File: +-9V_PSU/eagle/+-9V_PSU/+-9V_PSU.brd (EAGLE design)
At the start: 93.7 x 71.1 mm, 24 parts, among them IC1 7809TV, IC2 7909TV

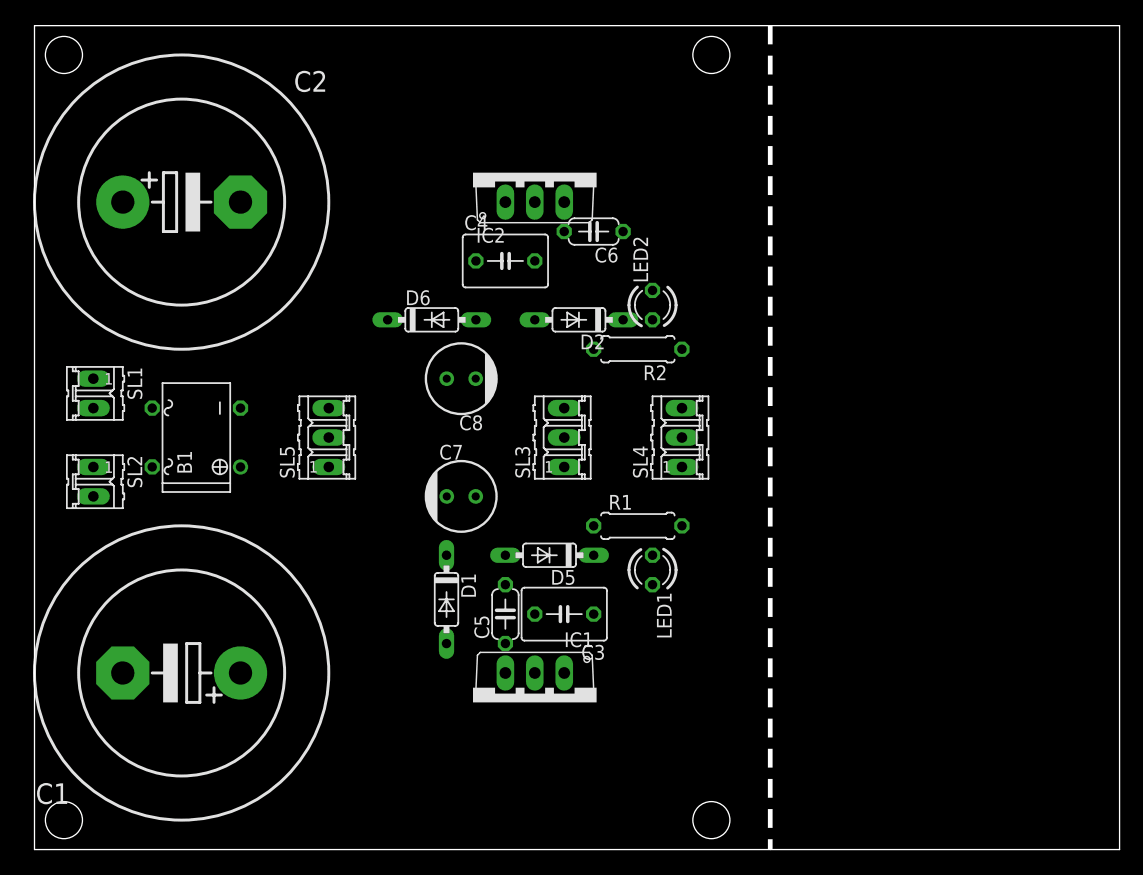
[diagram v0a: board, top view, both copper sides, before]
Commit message: +-9V PSU Board design
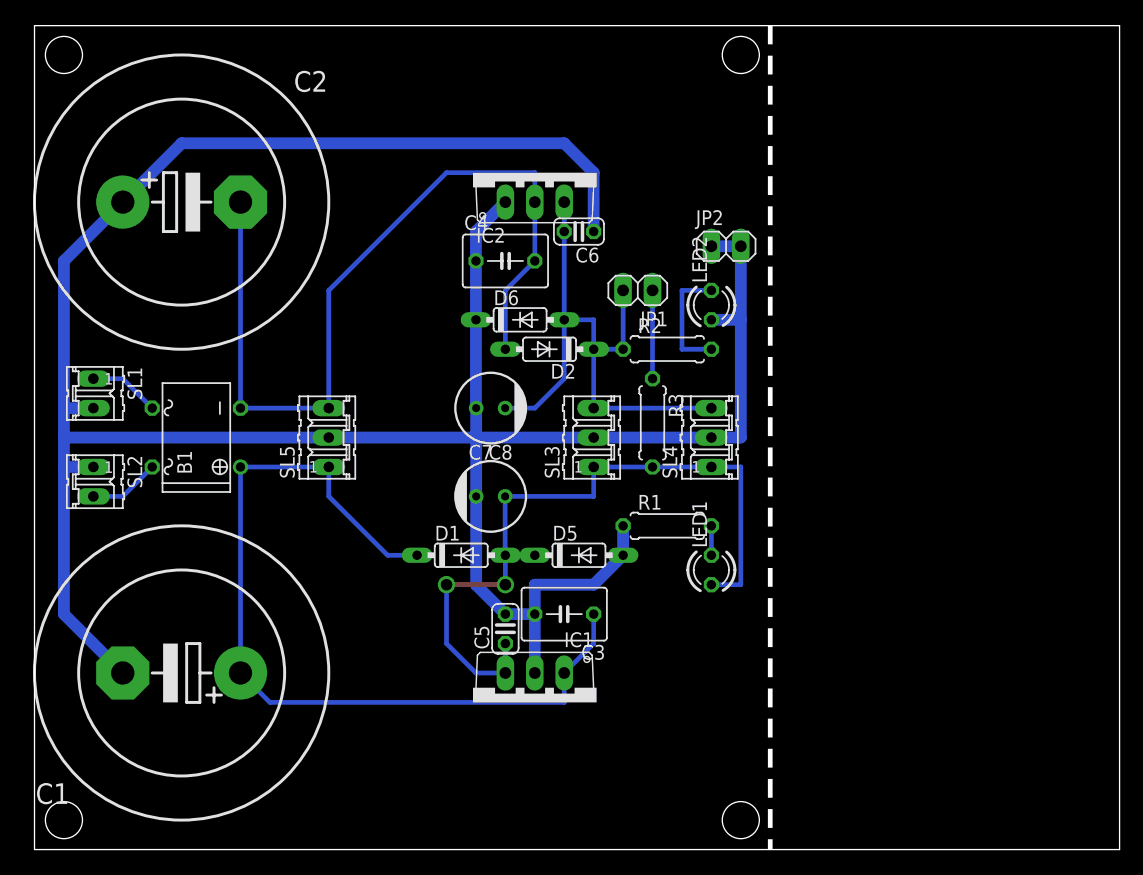
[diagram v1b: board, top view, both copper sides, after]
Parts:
- added JP1: LED, pinhead:1X02
- added JP2: TP_GND, pinhead:1X02
- added R3: 10k, rcl:0207/7
- C5, C6: device rcl:C050-024X044 -> rcl:C025-024X044
- SL1: value (none) -> ACIN1
- SL2: value (none) -> ACIN2
- SL3, SL4: value (none) -> DC9V
- SL5: value (none) -> DC12V
- moved D6 7.62 mm to (41.9, 45.7)
- moved LED1 5.08 mm to (58.4, 24.1), turned to 90 degrees
- moved LED2 5.08 mm to (58.4, 47.0)
- moved D1 4.02 mm to (36.8, 25.4), turned to 0 degrees
- moved C8 3.59 mm to (39.4, 38.1)
- moved D2 3.59 mm to (44.5, 43.2)
- moved C7 2.54 mm to (39.4, 30.5)
- moved D5 2.54 mm to (47.0, 25.4), turned to 0 degrees
- moved R1 2.54 mm to (54.6, 27.9)
- moved R2 2.54 mm to (54.6, 43.2), turned to 0 degrees
- moved SL3 2.54 mm to (48.3, 35.6)
- moved SL4 2.54 mm to (58.4, 35.6)
- moved C5 1.27 mm to (40.6, 19.1)
- moved C6 1.27 mm to (47.0, 53.3)
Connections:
- new net N$2: JP1.1, R3.1
- net +9V: now also R3.2
- net -9V: now also JP1.2, R2.1; no longer LED2.K
- net GND: now also JP2.1, JP2.2, LED2.A; no longer R2.2
- net N$1: now also LED2.K, R2.2; no longer LED2.A, R2.1
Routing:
- net GND: track 0.00 -> 237.9 mm
- net +12V: track 0.00 -> 75.3 mm
- net -12V: track 0.00 -> 73.8 mm
- net +9V: track 0.00 -> 64.6 mm, vias 0 -> 2
- net -9V: track 0.00 -> 49.3 mm
- net N$1: track 0.00 -> 10.2 mm
- net N$2: track 0.00 -> 7.62 mm
- net N$6: track 0.00 -> 6.13 mm
- net N$4: track 0.00 -> 6.13 mm
- net N$3: track 0.00 -> 2.54 mm

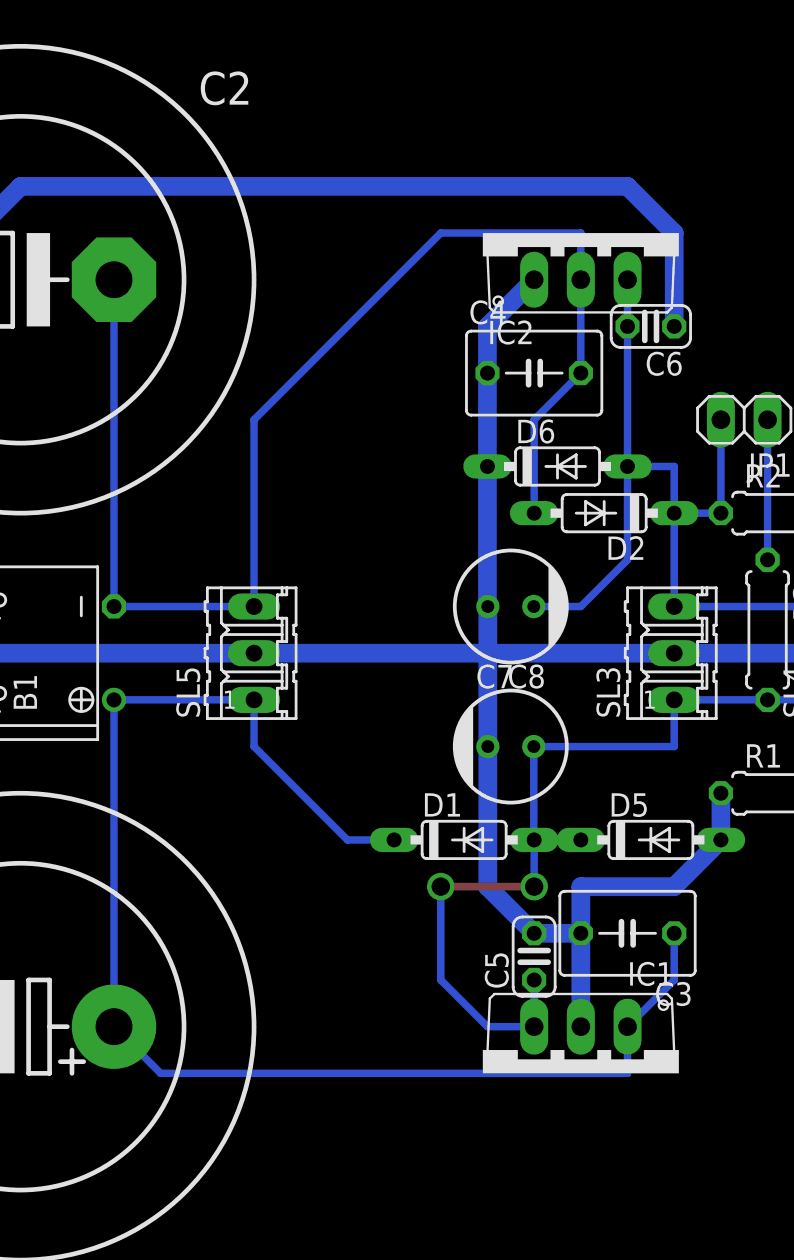
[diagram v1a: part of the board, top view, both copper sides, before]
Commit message: +-9V_PSU Update
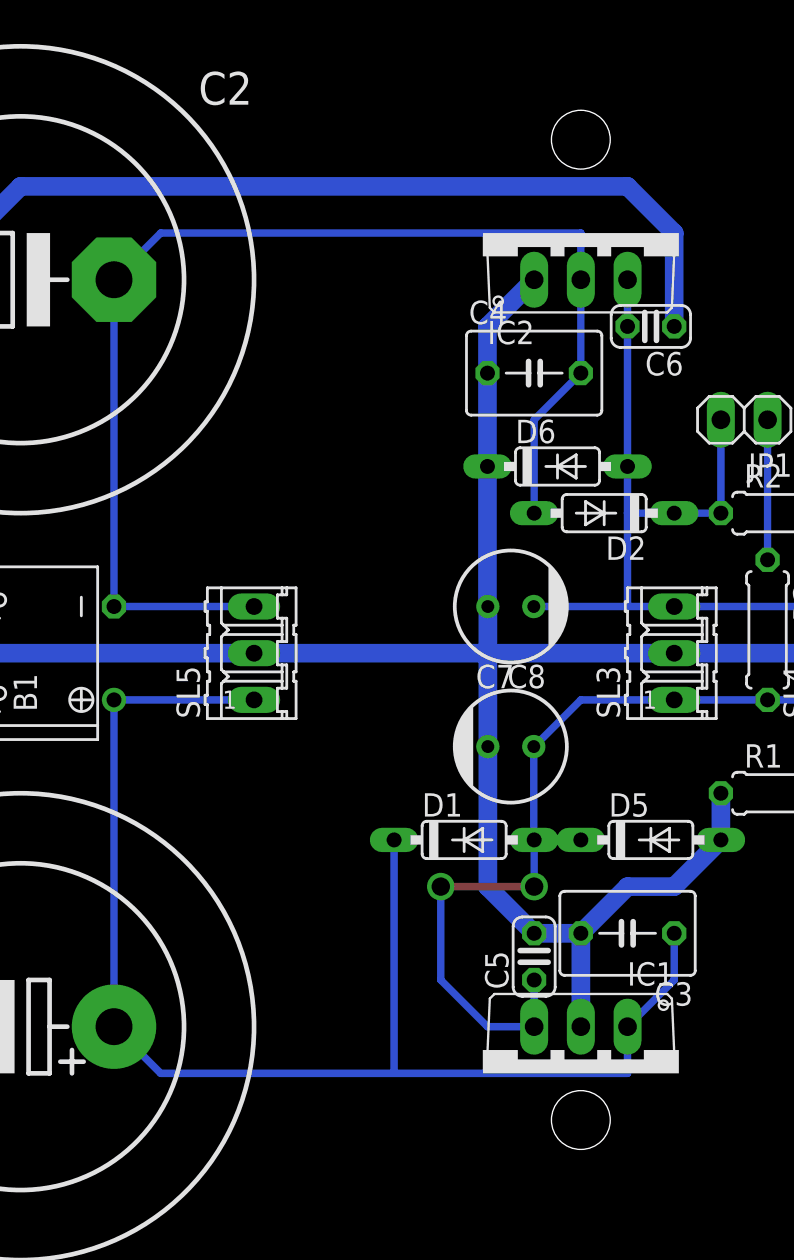
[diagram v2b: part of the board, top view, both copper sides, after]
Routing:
- net -12V: track 73.8 -> 68.1 mm
- net -9V: track 49.3 -> 45.7 mm
- net GND: track 237.9 -> 236.4 mm
- net +9V: track 64.6 -> 63.1 mm
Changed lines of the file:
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@@
 <layer number="98" name="Guide" color="6" fill="1" visible="no" active="no"/>
 <layer number="99" name="SpiceOrder" color="5" fill="1" visible="no" active="no"/>
-<layer number="100" name="Grid" color="11" fill="1" visible="yes" active="yes"/>
+<layer number="100" name="Grid" color="11" fill="1" visible="no" active="yes"/>
 <layer number="200" name="200bmp" color="1" fill="10" visible="no" active="no"/>
 <layer number="201" name="tNamesOnPCB" color="5" fill="1" visible="yes" active="yes"/>
@@
 <hole x="60.96" y="2.54" drill="3.2"/>
 <dimension x1="0" y1="0" x2="63.5" y2="0" x3="31.75" y3="-5.08" textsize="1.778" layer="20"/>
+<hole x="43.18" y="10.16" drill="3.2"/>
+<hole x="43.18" y="63.5" drill="3.2"/>
 </plain>
 <attributes>
@@
 <wire x1="45.72" y1="60.96" x2="12.7" y2="60.96" width="1.016" layer="16"/>
 <wire x1="12.7" y1="60.96" x2="7.62" y2="55.88" width="1.016" layer="16"/>
-<wire x1="43.18" y1="20.32" x2="43.18" y2="22.86" width="1.016" layer="16"/>
-<wire x1="43.18" y1="22.86" x2="48.26" y2="22.86" width="1.016" layer="16"/>
 <wire x1="48.26" y1="22.86" x2="50.8" y2="25.4" width="1.016" layer="16"/>
 <contactref element="LED2" pad="A"/>
@@
 <wire x1="58.42" y1="52.07" x2="60.96" y2="52.07" width="1.016" layer="16"/>
 <wire x1="60.96" y1="52.07" x2="60.96" y2="45.72" width="1.016" layer="16"/>
+<wire x1="43.18" y1="20.32" x2="45.72" y2="22.86" width="1.016" layer="16"/>
+<wire x1="45.72" y1="22.86" x2="48.26" y2="22.86" width="1.016" layer="16"/>
 </signal>
 <signal name="-9V">
@@
 <wire x1="45.72" y1="55.88" x2="45.72" y2="53.34" width="0.4064" layer="16"/>
 <wire x1="45.72" y1="45.72" x2="45.72" y2="53.34" width="0.4064" layer="16"/>
-<wire x1="40.62" y1="38.1" x2="43.18" y2="38.1" width="0.4064" layer="16"/>
-<wire x1="43.18" y1="38.1" x2="45.72" y2="40.64" width="0.4064" layer="16"/>
-<wire x1="45.72" y1="40.64" x2="45.72" y2="45.72" width="0.4064" layer="16"/>
+<wire x1="45.72" y1="43.18" x2="45.72" y2="45.72" width="0.4064" layer="16"/>
 <wire x1="48.26" y1="38.1" x2="58.42" y2="38.1" width="0.4064" layer="16"/>
 <contactref element="R2" pad="1"/>
-<wire x1="45.72" y1="45.72" x2="48.26" y2="45.72" width="0.4064" layer="16"/>
-<wire x1="48.26" y1="45.72" x2="48.26" y2="43.18" width="0.4064" layer="16"/>
-<wire x1="48.26" y1="43.18" x2="48.26" y2="38.1" width="0.4064" layer="16"/>
 <contactref element="JP1" pad="2"/>
 <wire x1="50.8" y1="43.18" x2="50.8" y2="48.26" width="0.4064" layer="16"/>
 <wire x1="50.8" y1="43.18" x2="48.26" y2="43.18" width="0.4064" layer="16"/>
+<wire x1="48.26" y1="43.18" x2="45.72" y2="43.18" width="0.4064" layer="16"/>
+<wire x1="48.26" y1="38.1" x2="45.72" y2="38.1" width="0.4064" layer="16"/>
+<wire x1="45.72" y1="38.1" x2="40.62" y2="38.1" width="0.4064" layer="16"/>
+<wire x1="45.72" y1="43.18" x2="45.72" y2="38.1" width="0.4064" layer="16"/>
 </signal>
 <signal name="+9V">
@@
 <wire x1="40.62" y1="30.48" x2="40.62" y2="25.42" width="0.4064" layer="16"/>
 <wire x1="40.62" y1="25.42" x2="40.64" y2="25.4" width="0.4064" layer="16"/>
-<wire x1="40.62" y1="30.48" x2="48.26" y2="30.48" width="0.4064" layer="16"/>
-<wire x1="48.26" y1="30.48" x2="48.26" y2="33.02" width="0.4064" layer="16"/>
 <wire x1="43.18" y1="25.4" x2="40.64" y2="25.4" width="0.4064" layer="16"/>
 <contactref element="R3" pad="2"/>
@@
 <via x="40.64" y="22.86" extent="1-16" drill="1" shape="square"/>
 <via x="35.56" y="22.86" extent="1-16" drill="1" shape="square"/>
+<wire x1="40.62" y1="30.48" x2="40.64" y2="30.48" width="0.4064" layer="16"/>
+<wire x1="40.64" y1="30.48" x2="43.18" y2="33.02" width="0.4064" layer="16"/>
+<wire x1="43.18" y1="33.02" x2="48.26" y2="33.02" width="0.4064" layer="16"/>
 </signal>
 <signal name="N$3">
@@
 <wire x1="17.78" y1="33.02" x2="25.4" y2="33.02" width="0.4064" layer="16"/>
 <wire x1="17.78" y1="15.24" x2="20.32" y2="12.7" width="0.4064" layer="16"/>
-<wire x1="20.32" y1="12.7" x2="45.72" y2="12.7" width="0.4064" layer="16"/>
+<wire x1="20.32" y1="12.7" x2="33.02" y2="12.7" width="0.4064" layer="16"/>
+<wire x1="33.02" y1="12.7" x2="45.72" y2="12.7" width="0.4064" layer="16"/>
 <wire x1="45.72" y1="12.7" x2="45.72" y2="15.24" width="0.4064" layer="16"/>
 <wire x1="17.78" y1="15.24" x2="17.78" y2="33.02" width="0.4064" layer="16"/>
-<wire x1="25.4" y1="33.02" x2="25.4" y2="30.48" width="0.4064" layer="16"/>
-<wire x1="25.4" y1="30.48" x2="30.48" y2="25.4" width="0.4064" layer="16"/>
-<wire x1="30.48" y1="25.4" x2="33.02" y2="25.4" width="0.4064" layer="16"/>
+<wire x1="33.02" y1="25.4" x2="33.02" y2="12.7" width="0.4064" layer="16"/>
 </signal>
 <signal name="-12V">
@@
 <wire x1="17.78" y1="38.1" x2="25.4" y2="38.1" width="0.4064" layer="16"/>
 <wire x1="43.18" y1="55.88" x2="43.18" y2="58.42" width="0.4064" layer="16"/>
-<wire x1="43.18" y1="58.42" x2="35.56" y2="58.42" width="0.4064" layer="16"/>
-<wire x1="35.56" y1="58.42" x2="25.4" y2="48.26" width="0.4064" layer="16"/>
-<wire x1="25.4" y1="48.26" x2="25.4" y2="38.1" width="0.4064" layer="16"/>
 <wire x1="43.18" y1="55.88" x2="43.18" y2="50.8" width="0.4064" layer="16"/>
 <wire x1="40.64" y1="43.18" x2="40.64" y2="48.26" width="0.4064" layer="16"/>
 <wire x1="40.64" y1="48.26" x2="43.18" y2="50.8" width="0.4064" layer="16"/>
+<wire x1="43.18" y1="58.42" x2="20.32" y2="58.42" width="0.4064" layer="16"/>
+<wire x1="20.32" y1="58.42" x2="17.78" y2="55.88" width="0.4064" layer="16"/>
 </signal>
 <signal name="N$1">
@@
 </signal>
 </signals>
+<errors>
+</errors>
 </board>
 </drawing>
